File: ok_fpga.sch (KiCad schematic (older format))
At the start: 32 parts

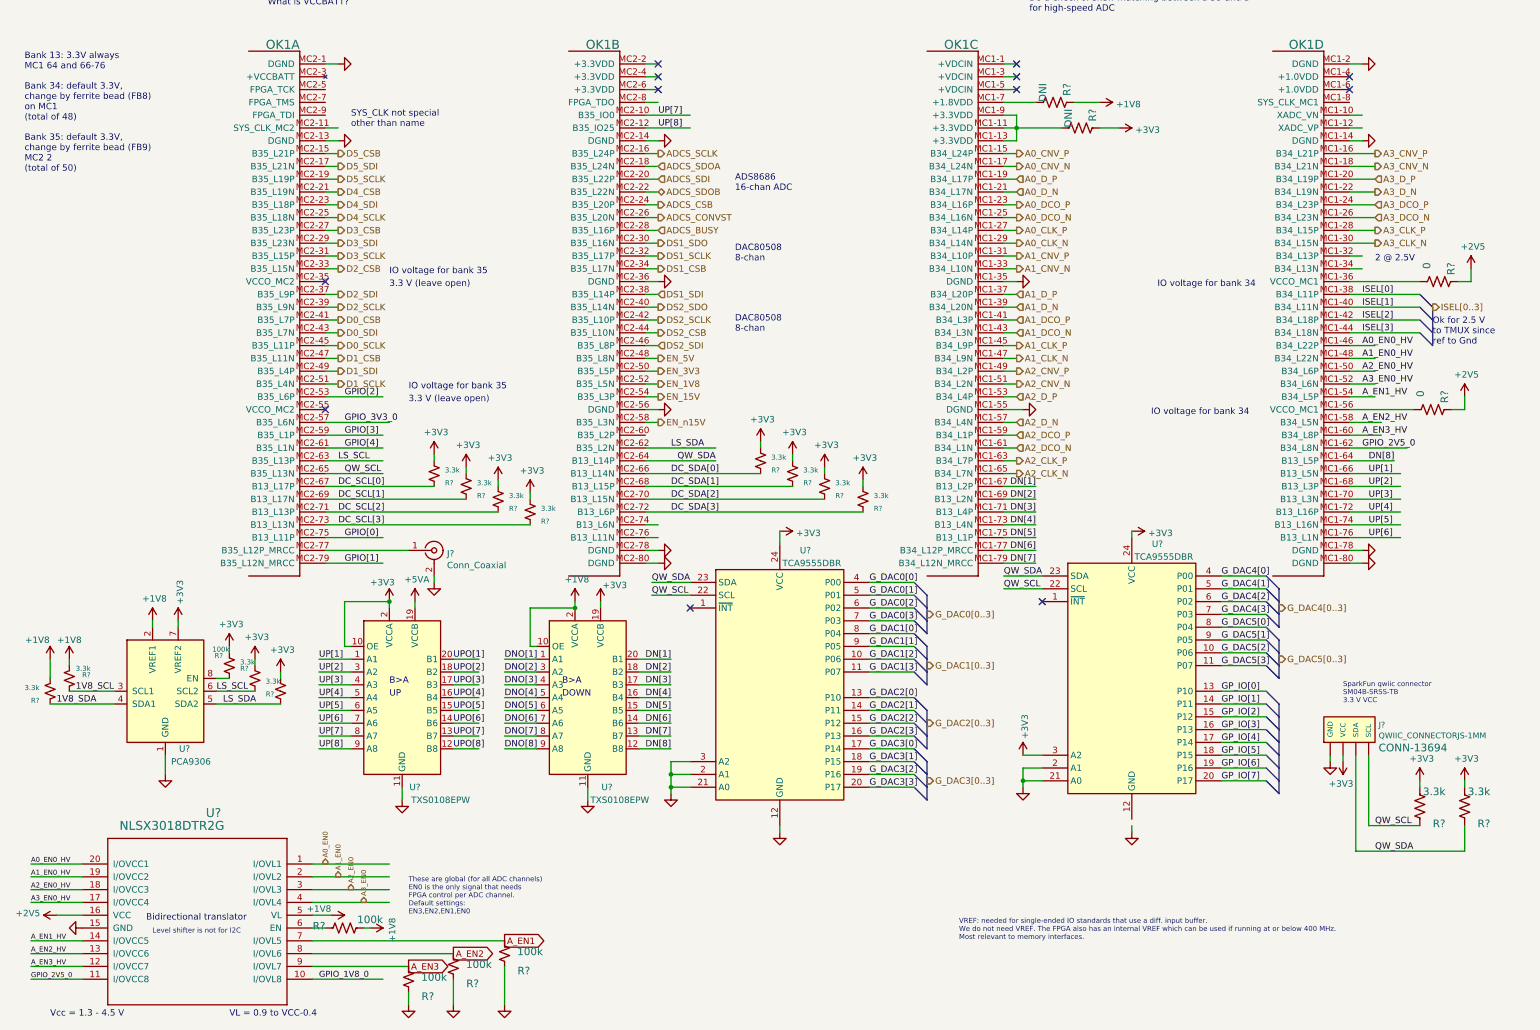
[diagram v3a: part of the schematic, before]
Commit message: near complete top level schematic routing
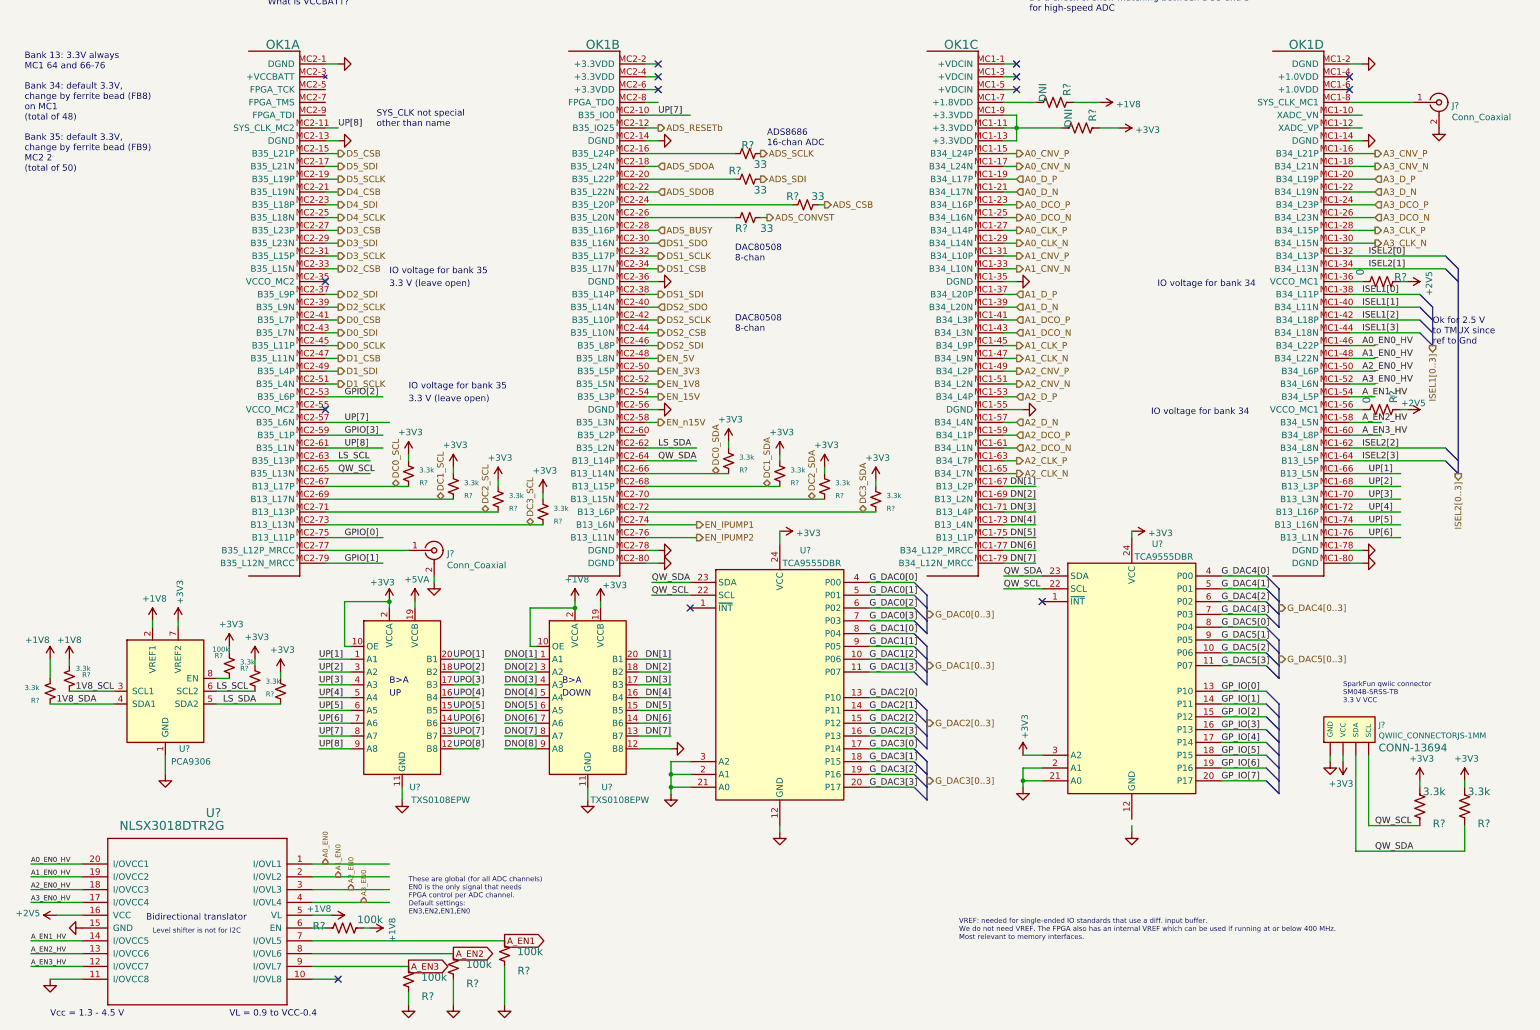
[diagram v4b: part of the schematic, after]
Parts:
- removed R? (x4): 3.3k, Resistor_SMD:R_0603_1608Metric, symbol Device:R_Small_US
- added J?: Conn_Coaxial, symbol Connector:Conn_Coaxial
- added R? (x4): 33, Resistor_SMD:R_0603_1608Metric, symbol Device:R_Small_US
- added R? (x4): 3.3k, Resistor_SMD:R_0603_1608Metric, symbol Device:R_Small_US
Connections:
- net labels added: ADS_BUSY, ADS_CONVST, ADS_CSB, ADS_RESETb, ADS_SCLK, ADS_SDI, ADS_SDOA, ADS_SDOB, DC0_SCL, DC0_SDA, DC1_SCL, DC1_SDA, DC2_SCL, DC2_SDA, DC3_SCL, DC3_SDA, EN_IPUMP1, EN_IPUMP2, ISEL1[0..3], ISEL1[0], ISEL1[1], ISEL1[2], ISEL1[3], ISEL2[0..3], ISEL2[0], ISEL2[1], ISEL2[2], ISEL2[3]
- net labels removed: ADCS_BUSY, ADCS_CONVST, ADCS_CSB, ADCS_SCLK, ADCS_SDI, ADCS_SDOA, ADCS_SDOB, DC_SCL[0], DC_SCL[1], DC_SCL[2], DC_SCL[3], DC_SDA[0], DC_SDA[1], DC_SDA[2], DC_SDA[3], DN[8], GPIO[4], GPIO_1V8_0, GPIO_2V5_0, GPIO_3V3_0, ISEL[0..3], ISEL[0], ISEL[1], ISEL[2], ISEL[3]
- wire segments 308 -> 309
- no-connect marks 12 -> 13
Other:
- note removed: "2 @ 2.5V"
- moved on the sheet: R?

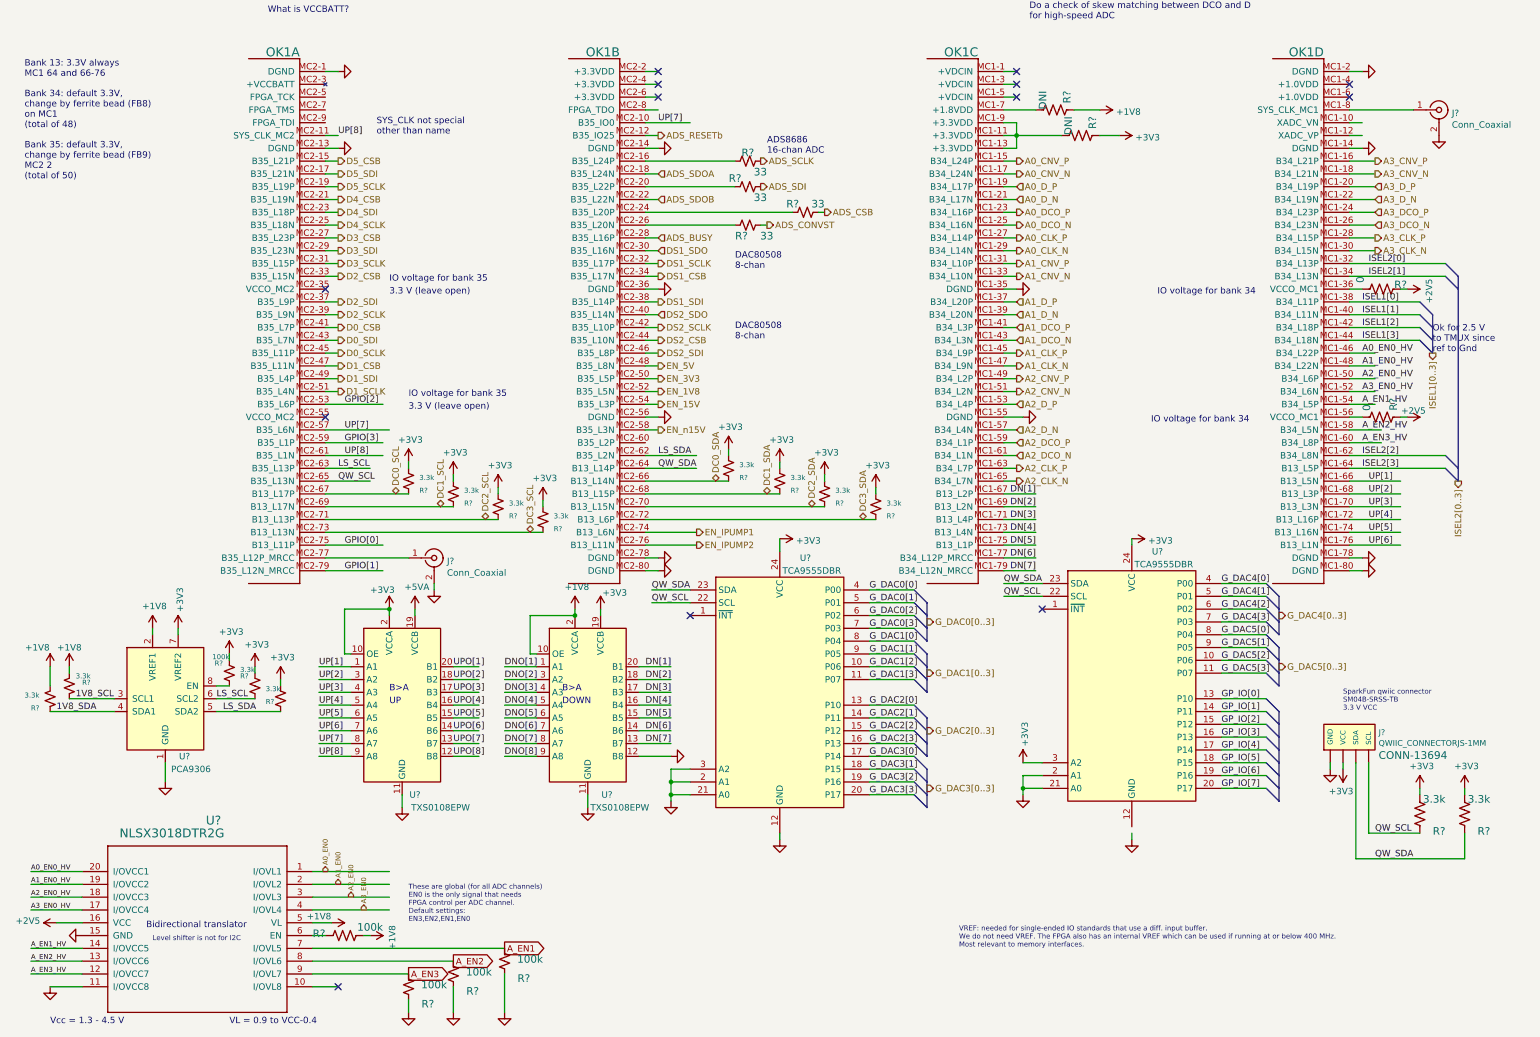
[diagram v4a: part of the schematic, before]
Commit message: corrected most ERC errors
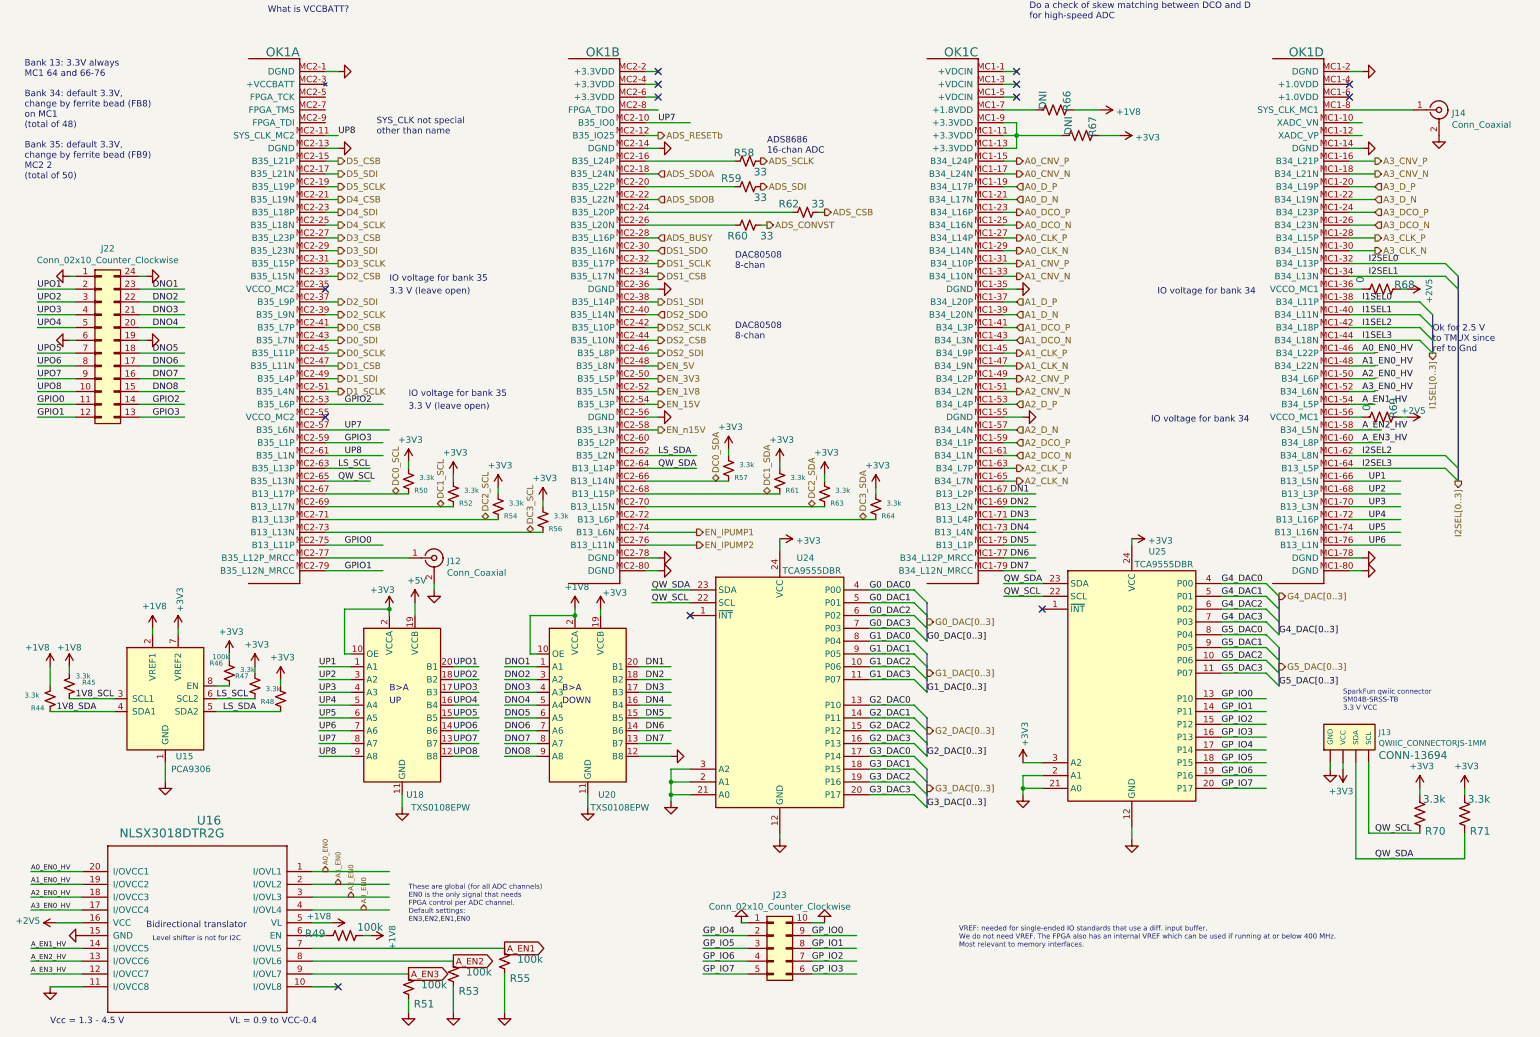
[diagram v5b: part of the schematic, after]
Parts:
- added J22: Conn_02x10_Counter_Clockwise, symbol Connector_Generic:Conn_02x12_Counter_Clockwise
- added J23: Conn_02x10_Counter_Clockwise, symbol Connector_Generic:Conn_02x05_Counter_Clockwise
- J13: renamed from J?; footprint 1X04_1MM_RA -> Connectors:1X04_1MM_RA
- gave numbers to parts that had none: 35
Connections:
- net labels added: +5V, DN1, DN2, DN3, DN4, DN5, DN6, DN7, DNO1, DNO2, DNO3, DNO4, DNO5, DNO6, DNO7, DNO8, G0_DAC0, G0_DAC1, G0_DAC2, G0_DAC3, G0_DAC[0..3], G1_DAC0, G1_DAC1, G1_DAC2, G1_DAC3, G1_DAC[0..3], G2_DAC0, G2_DAC1, G2_DAC2, G2_DAC3, G2_DAC[0..3], G3_DAC0, G3_DAC1, G3_DAC2, G3_DAC3, G3_DAC[0..3], G4_DAC0, G4_DAC1, G4_DAC2, G4_DAC3, G4_DAC[0..3], G5_DAC0, G5_DAC1, G5_DAC2, G5_DAC3, G5_DAC[0..3], GPIO0, GPIO1, GPIO2, GPIO3, GP_IO0, GP_IO1, GP_IO2, GP_IO3, GP_IO4, GP_IO5, GP_IO6, GP_IO7, I1SEL0, I1SEL1, I1SEL2, I1SEL3, I1SEL[0..3], I2SEL0, I2SEL1, I2SEL2, I2SEL3, I2SEL[0..3], UP1, UP2, UP3, UP4, UP5, UP6, UP7, UP8, UPO1, UPO2, UPO3, UPO4, UPO5, UPO6, UPO7, UPO8
- net labels removed: +5VA, DNO[1], DNO[2], DNO[3], DNO[4], DNO[5], DNO[6], DNO[7], DNO[8], DN[1], DN[2], DN[3], DN[4], DN[5], DN[6], DN[7], GPIO[0], GPIO[1], GPIO[2], GPIO[3], GP_IO[0], GP_IO[1], GP_IO[2], GP_IO[3], GP_IO[4], GP_IO[5], GP_IO[6], GP_IO[7], G_DAC0[0..3], G_DAC0[0], G_DAC0[1], G_DAC0[2], G_DAC0[3], G_DAC1[0..3], G_DAC1[0], G_DAC1[1], G_DAC1[2], G_DAC1[3], G_DAC2[0..3], G_DAC2[0], G_DAC2[1], G_DAC2[2], G_DAC2[3], G_DAC3[0..3], G_DAC3[0], G_DAC3[1], G_DAC3[2], G_DAC3[3], G_DAC4[0..3], G_DAC4[0], G_DAC4[1], G_DAC4[2], G_DAC4[3], G_DAC5[0..3], G_DAC5[0], G_DAC5[1], G_DAC5[2], G_DAC5[3], ISEL1[0..3], ISEL1[0], ISEL1[1], ISEL1[2], ISEL1[3], ISEL2[0..3], ISEL2[0], ISEL2[1], ISEL2[2], ISEL2[3], UPO[1], UPO[2], UPO[3], UPO[4], UPO[5], UPO[6], UPO[7], UPO[8], UP[1], UP[2], UP[3], UP[4], UP[5], UP[6], UP[7], UP[8]
- wire segments 309 -> 343

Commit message: after using kifield to update Manf#
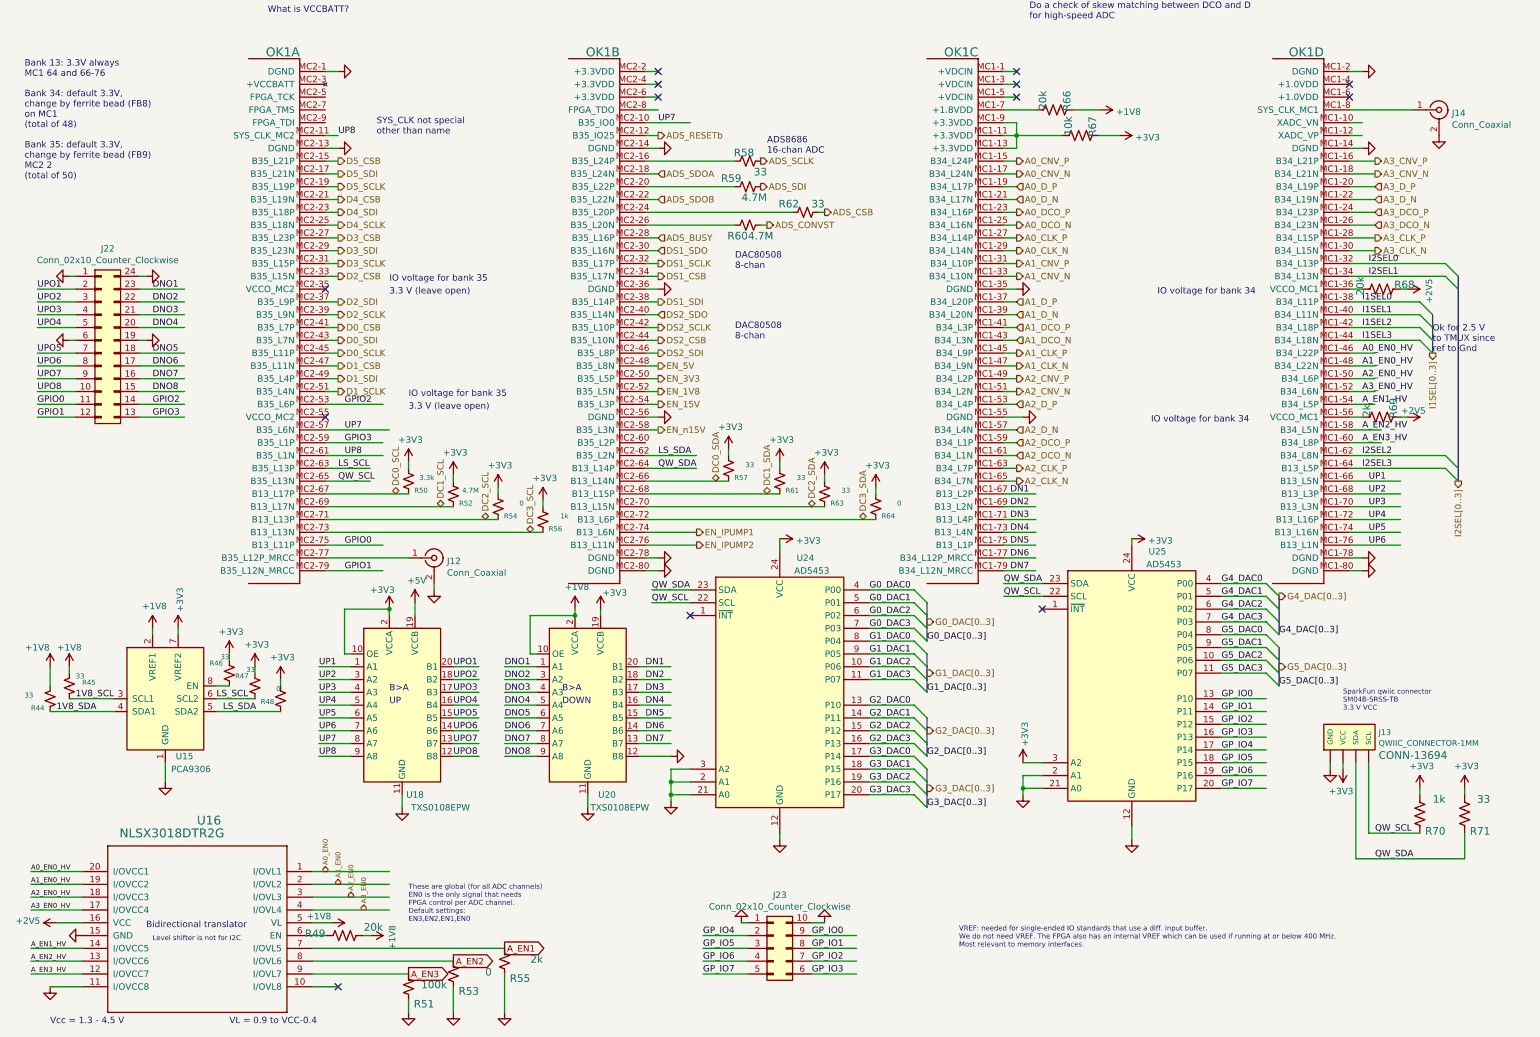
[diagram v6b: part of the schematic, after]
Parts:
- J13: value QWIIC_CONNECTORJS-1MM -> QWIIC_CONNECTOR-1MM; Manf# (none) -> PRT-14417
- OK1: Manf# (none) -> BTE-040-02-F-D-A
- R44, R45, R47, R57, R61, R63, R71: value 3.3k -> 33; Manf# (none) -> RC0603FR-0733RL; Power (none) -> 0.1W; Tolerance (none) -> 1%
- R46: value 100k -> 33; Manf# (none) -> RC0603FR-0733RL; Power (none) -> 0.1W; Tolerance (none) -> 1%
- R48, R54, R64: value 3.3k -> 0; Manf# (none) -> RC0603FR-070RL; Power (none) -> 0.1W
- R49: value 100k -> 20k; Manf# (none) -> RC0603FR-0720KL; Power (none) -> 0.1W; Tolerance (none) -> 1%
- R50: Manf# (none) -> RC0603FR-073k3L; Power (none) -> 0.1W; Tolerance (none) -> 1%
- R51: Manf# (none) -> RC0603FR-07100KL; Power (none) -> 0.1W; Tolerance (none) -> 1%
- R52: value 3.3k -> 4.7M; footprint Resistor_SMD:R_0603_1608Metric -> Resistor_SMD:R_1206_3216Metric; Manf# (none) -> RG3216P-4704-B-T1; Tolerance (none) -> 0.1
- R53: value 100k -> 0; Manf# (none) -> RC0603FR-070RL; Power (none) -> 0.1W
- R55: value 100k -> 2k; Manf# (none) -> RC0603FR-072KL; Power (none) -> 0.1W; Tolerance (none) -> 1%
- R56, R70: value 3.3k -> 1k; Manf# (none) -> RC0603FR-071KL; Power (none) -> 0.1W; Tolerance (none) -> 1%
- R58, R62: Manf# (none) -> RC0603FR-0733RL; Power (none) -> 0.1W; Tolerance (none) -> 1%
- R59, R60: value 33 -> 4.7M; footprint Resistor_SMD:R_0603_1608Metric -> Resistor_SMD:R_1206_3216Metric; Manf# (none) -> RG3216P-4704-B-T1; Tolerance (none) -> 0.1
- R66: value DNI -> 20k; Manf# (none) -> RC0603FR-0720KL; Power (none) -> 0.1W; Tolerance (none) -> 1%
- R67: value DNI -> 10k; Manf# (none) -> RC0603FR-0710kL; Power (none) -> 0.1W; Tolerance (none) -> 1%
- R68: value 0 -> 20k; Manf# (none) -> RC0603FR-0720KL; Power (none) -> 0.1W; Tolerance (none) -> 1%
- R69: value 0 -> 2k; Manf# (none) -> RC0603FR-072KL; Power (none) -> 0.1W; Tolerance (none) -> 1%
- U15: Description (none) -> IC TRNSLTR BIDIRECTIONAL 8TSSOP; Manf# (none) -> PCA9306DTR2G
- U16: Manf# (none) -> NLSX3018DTR2G
- U18, U20: Manf# (none) -> TXS0108EPWR
- U24, U25: value TCA9555DBR -> AD5453; footprint Package_SO:SSOP-24_5.3x8.2mm_P0.65mm -> adc_dac_v1:RM_8; Manf# (none) -> AD5453YRMZ-REEL7
